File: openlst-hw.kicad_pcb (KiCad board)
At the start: 4 copper layers, 60 x 50 mm, 94 parts, among them J1 5VDC, J2 CC Prog/Debug, J3 UART0, J4 UART1, J5 Control Outputs, J6 ANT, U1 LM1117-3.3, U2 CC1110, U3 LT1086-3.6, U4 FOX924 27MHz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

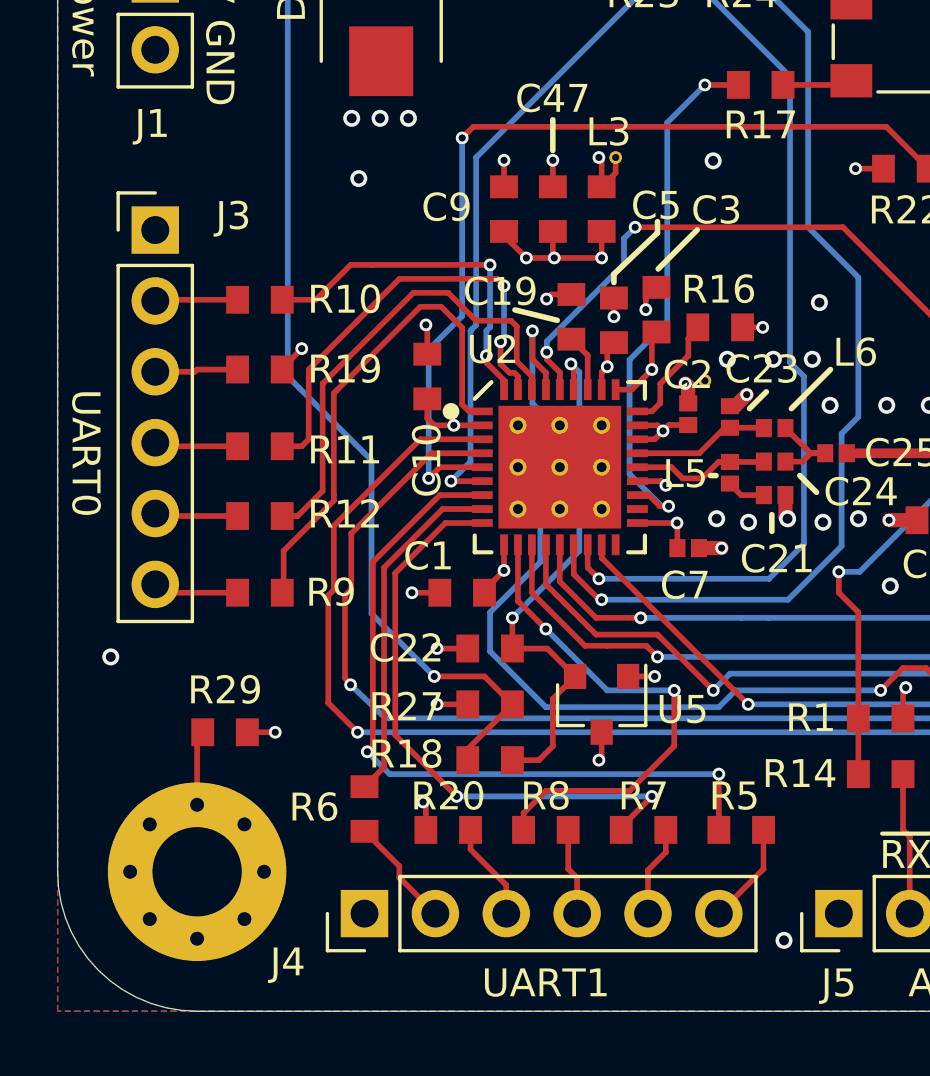
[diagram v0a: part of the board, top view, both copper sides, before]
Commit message: Silkscreen labels for UART pins
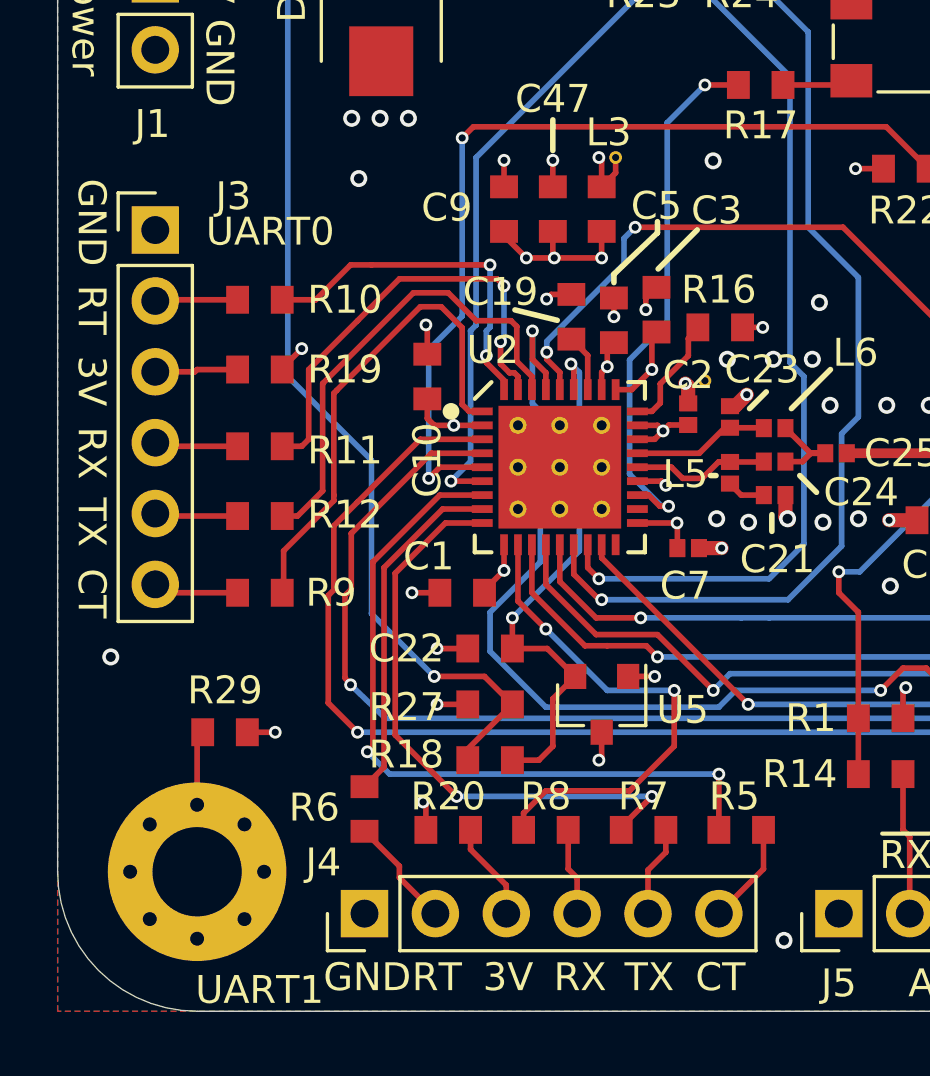
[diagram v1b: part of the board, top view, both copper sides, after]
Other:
- board text added: "3V"
- board text added: "CT"
- board text added: "RT"
- board text added: "RX"
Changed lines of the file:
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@@
     (tags "Through hole pin header THT 1x06 2.54mm single row")
     (attr through_hole)
-    (fp_text reference "J3" (at 2.8 -0.5 180) (layer "F.SilkS")
+    (fp_text reference "J3" (at 2.8 -1.21 180) (layer "F.SilkS")
         (effects (font (size 1 1) (thickness 0.15)))
     )
@@
     (tags "Through hole pin header THT 1x06 2.54mm single row")
     (attr through_hole)
-    (fp_text reference "J4" (at -1.75 -2.75) (layer "F.SilkS")
+    (fp_text reference "J4" (at 1.834 -1.475) (layer "F.SilkS")
         (effects (font (size 1 1) (thickness 0.15)))
     )
@@
     (effects (font (size 1 1) (thickness 0.15)))
   )
-  (gr_text "UART0" (at 114.5 68.5 270) (layer "F.SilkS")
+  (gr_text "UART0" (at 121.12 60.56) (layer "F.SilkS")
     (effects (font (size 1 1) (thickness 0.15)))
+  )
+  (gr_text "TX" (at 114.135 70.085 -90) (layer "F.SilkS")
+    (effects (font (size 1 1) (thickness 0.15)) (justify left bottom))
+  )
+  (gr_text "3V" (at 114.135 65.005 -90) (layer "F.SilkS")
+    (effects (font (size 1 1) (thickness 0.15)) (justify left bottom))
+  )
+  (gr_text "CT" (at 136.36 87.865) (layer "F.SilkS")
+    (effects (font (size 1 1) (thickness 0.15)) (justify left bottom))
+  )
+  (gr_text "CT" (at 114.135 72.625 -90) (layer "F.SilkS")
+    (effects (font (size 1 1) (thickness 0.15)) (justify left bottom))
+  )
+  (gr_text "TX" (at 133.82 87.865) (layer "F.SilkS")
+    (effects (font (size 1 1) (thickness 0.15)) (justify left bottom))
   )
   (gr_text "rev 2.2, 2023-09-11" (at 156.7 87.5) (layer "F.SilkS")
     (effects (font (size 1 1) (thickness 0.15)))
   )
+  (gr_text "RX" (at 131.28 87.865) (layer "F.SilkS")
+    (effects (font (size 1 1) (thickness 0.15)) (justify left bottom))
+  )
   (gr_text "OpenLST" (at 156.5 84.5) (layer "F.SilkS")
     (effects (font (size 2.5 2.5) (thickness 0.45) italic))
   )
+  (gr_text "RT" (at 126.2 87.865) (layer "F.SilkS")
+    (effects (font (size 1 1) (thickness 0.15)) (justify left bottom))
+  )
   (gr_text "Aux" (at 145.3 87.5) (layer "F.SilkS")
     (effects (font (size 1 1) (thickness 0.15)))
   )
-  (gr_text "UART1" (at 131 87.5) (layer "F.SilkS")
+  (gr_text "RX" (at 114.135 67.545 -90) (layer "F.SilkS")
+    (effects (font (size 1 1) (thickness 0.15)) (justify left bottom))
+  )
+  (gr_text "GND" (at 114.135 58.655 -90) (layer "F.SilkS")
+    (effects (font (size 1 1) (thickness 0.15)) (justify left bottom))
+  )
+  (gr_text "UART1" (at 120.739 87.738) (layer "F.SilkS")
     (effects (font (size 1 1) (thickness 0.15)))
   )
+  (gr_text "RT" (at 114.135 62.465 -90) (layer "F.SilkS")
+    (effects (font (size 1 1) (thickness 0.15)) (justify left bottom))
+  )
+  (gr_text "GND" (at 123.025 87.865) (layer "F.SilkS")
+    (effects (font (size 1 1) (thickness 0.15)) (justify left bottom))
+  )
+  (gr_text "3V" (at 128.74 87.865) (layer "F.SilkS")
+    (effects (font (size 1 1) (thickness 0.15)) (justify left bottom))
+  )
   (gr_text "Power" (at 114.5 52.9 270) (layer "F.SilkS")
